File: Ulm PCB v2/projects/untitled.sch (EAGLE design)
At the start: 26 parts, among them U1 FT232RLSSOP, U2 MCP73831, U3 SPX3819-3.3, X2 USB-SMD-NS

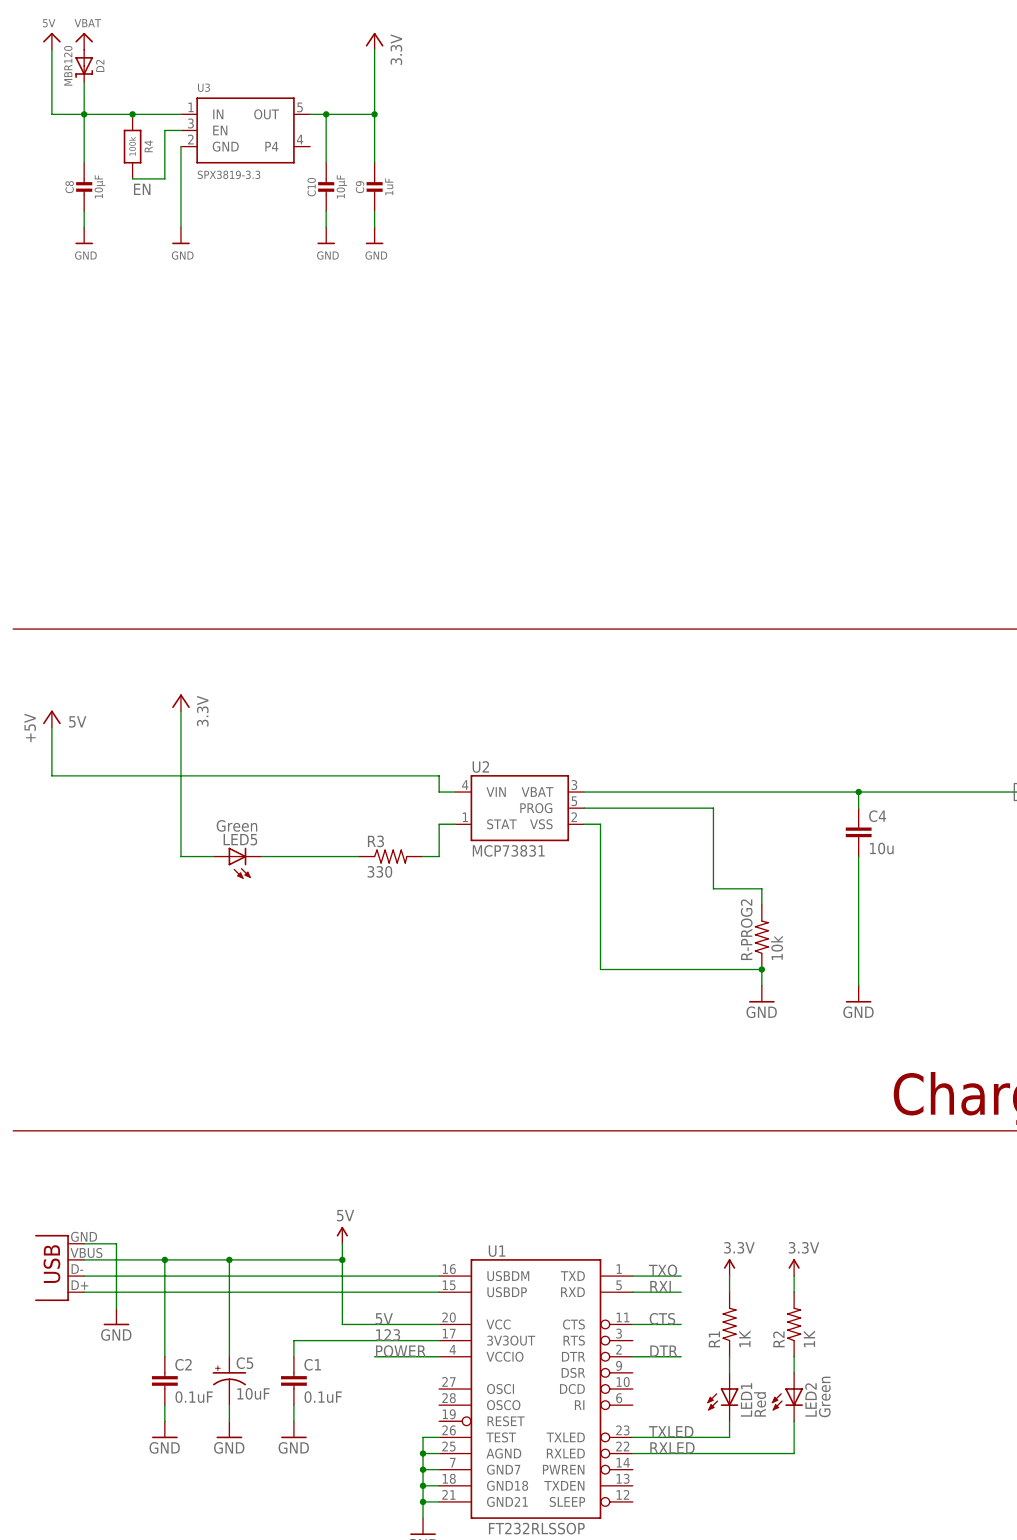
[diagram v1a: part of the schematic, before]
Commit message: replaced some parts with their bigger equivalent
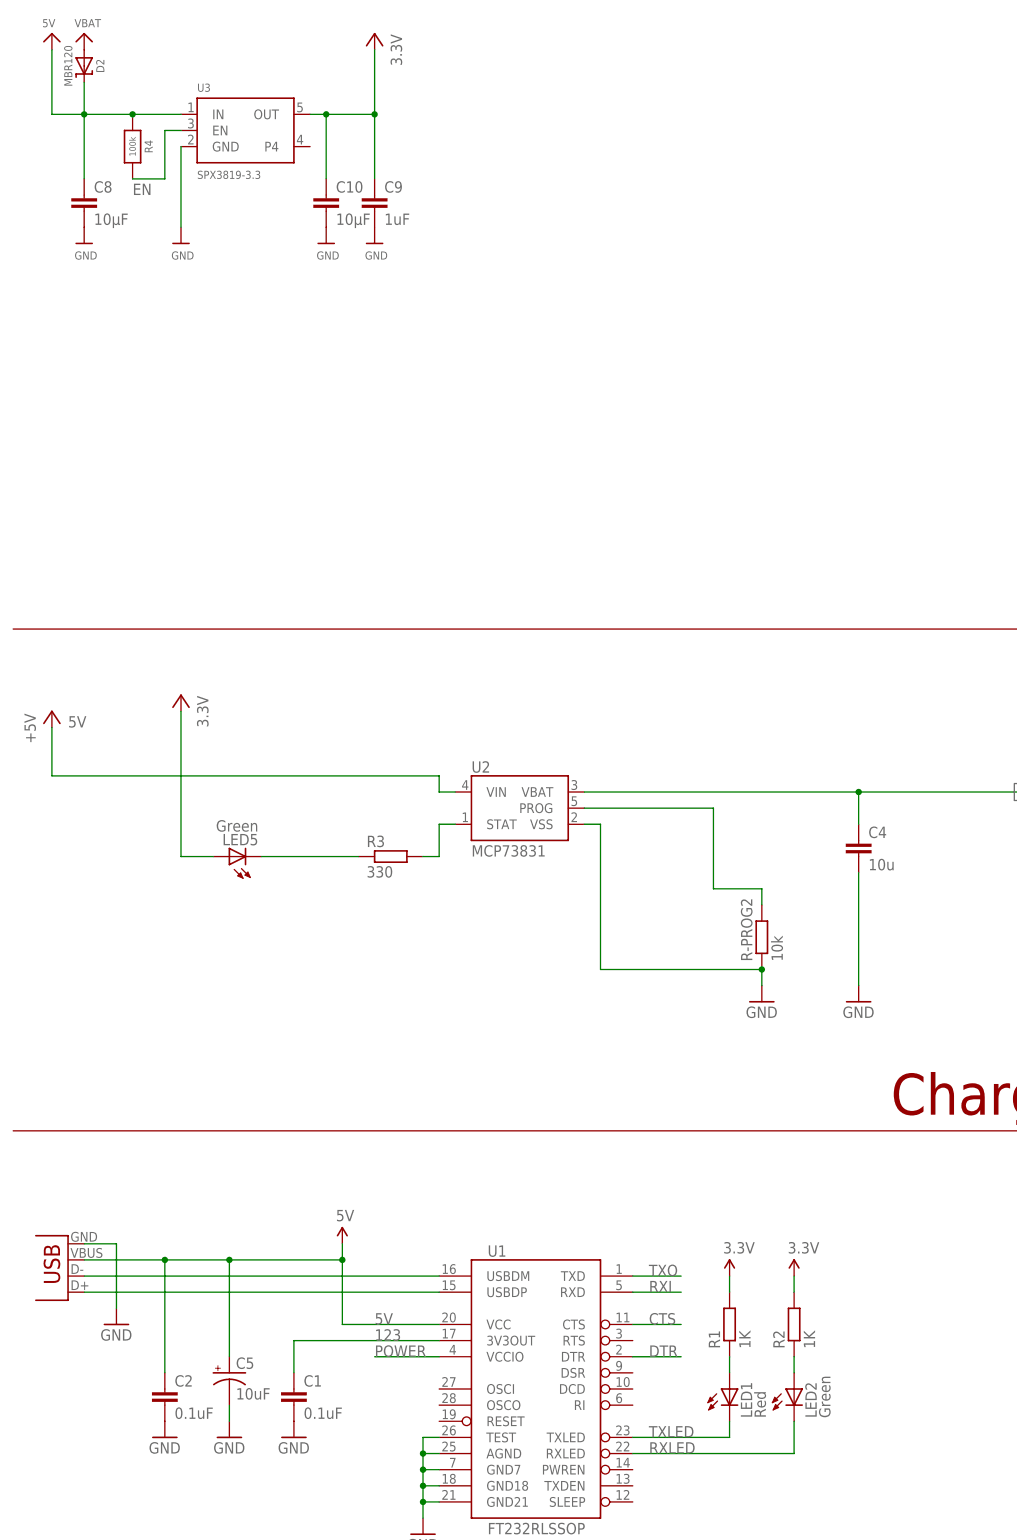
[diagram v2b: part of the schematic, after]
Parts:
- C1, C2: device SparkFun:CAP0402-CAP -> rcl:C-EUC0805
- C10, C8: device microbuilder:CAP_CERAMIC0805-NOOUTLINE -> rcl:C-EUC0805
- C4: device SparkFun-Capacitors:4.7UF-6.3V-10%(0603)0603 -> rcl:C-EUC0805
- C9: device microbuilder:CAP_CERAMIC0603_NO -> rcl:C-EUC0805
- R-PROG2: device SparkFun-Resistors:10KOHM1/10W1%(0603)0603 -> rcl:R-EU_R0603
- R1, R2: device SparkFun:RESISTOR0402-RES -> rcl:R-EU_R0603
- R3: device SparkFun-Resistors:330OHM1/10W1%(0603) -> rcl:R-EU_R0603
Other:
- moved on the sheet: C1, C10, C2, C4, C8, C9
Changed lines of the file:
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@@
 <part name="GND4" library="supply1" deviceset="GND" device=""/>
 <part name="GND6" library="supply1" deviceset="GND" device=""/>
-<part name="C2" library="SparkFun" deviceset="CAP" device="0402-CAP" value="0.1uF"/>
+<part name="C2" library="rcl" library_urn="urn:adsk.eagle:library:334" deviceset="C-EU" device="C0805" value="0.1uF"/>
 <part name="C5" library="SparkFun" deviceset="CAP_POL" device="1206" value="10uF"/>
-<part name="C1" library="SparkFun" deviceset="CAP" device="0402-CAP" value="0.1uF"/>
+<part name="C1" library="rcl" library_urn="urn:adsk.eagle:library:334" deviceset="C-EU" device="C0805" value="0.1uF"/>
 <part name="X2" library="SparkFun" deviceset="USB" device="-SMD-NS"/>
 <part name="GND2" library="SparkFun" deviceset="GND" device=""/>
@@
 <part name="GND7" library="SparkFun" deviceset="GND" device=""/>
 <part name="GND8" library="SparkFun" deviceset="GND" device=""/>
-<part name="R1" library="SparkFun" deviceset="RESISTOR" device="0402-RES" value="1K"/>
-<part name="R2" library="SparkFun" deviceset="RESISTOR" device="0402-RES" value="1K"/>
+<part name="R1" library="rcl" library_urn="urn:adsk.eagle:library:334" deviceset="R-EU_" device="R0603" value="1K"/>
+<part name="R2" library="rcl" library_urn="urn:adsk.eagle:library:334" deviceset="R-EU_" device="R0603" value="1K"/>
 <part name="LED1" library="SparkFun" deviceset="LED" device="0603" value="Red"/>
 <part name="LED2" library="SparkFun" deviceset="LED" device="0603" value="Green"/>
@@
 <part name="GND1" library="supply1" deviceset="GND" device=""/>
 <part name="U2" library="SparkFun-PowerIC" deviceset="MCP73831" device=""/>
-<part name="R3" library="SparkFun-Resistors" deviceset="330OHM1/10W1%(0603)" device="" value="330"/>
-<part name="C4" library="SparkFun-Capacitors" deviceset="4.7UF-6.3V-10%(0603)" device="0603" value="10u"/>
+<part name="R3" library="rcl" library_urn="urn:adsk.eagle:library:334" deviceset="R-EU_" device="R0603" value="330"/>
+<part name="C4" library="rcl" library_urn="urn:adsk.eagle:library:334" deviceset="C-EU" device="C0805" value="10u"/>
 <part name="GND12" library="SparkFun" deviceset="GND" device=""/>
-<part name="R-PROG2" library="SparkFun-Resistors" deviceset="10KOHM1/10W1%(0603)" device="0603" value="10k"/>
+<part name="R-PROG2" library="rcl" library_urn="urn:adsk.eagle:library:334" deviceset="R-EU_" device="R0603" value="10k"/>
 <part name="GND14" library="SparkFun" deviceset="GND" device=""/>
 <part name="FRAME1" library="frames" deviceset="A3L-LOC" device=""/>
@@
 <part name="GND9" library="supply1" deviceset="GND" device=""/>
 <part name="P+3" library="supply1" deviceset="VCC" device=""/>
-<part name="C6" library="rcl" deviceset="C-EU" device="C0805" value="100n"/>
+<part name="C6" library="rcl" library_urn="urn:adsk.eagle:library:334" deviceset="C-EU" device="C0805" value="100n"/>
 <part name="C7" library="rcl" deviceset="C-EU" device="C0805" value="100n"/>
 <part name="U$6" library="_c2h" deviceset="RFM95" device=""/>
@@
 <part name="GND13" library="supply1" deviceset="GND" device=""/>
 <part name="GND16" library="supply1" deviceset="GND" device=""/>
-<part name="C8" library="microbuilder" deviceset="CAP_CERAMIC" device="0805-NOOUTLINE" value="10µF"/>
-<part name="C9" library="microbuilder" deviceset="CAP_CERAMIC" device="0603_NO" value="1uF"/>
+<part name="C8" library="rcl" library_urn="urn:adsk.eagle:library:334" deviceset="C-EU" device="C0805" value="10µF"/>
+<part name="C9" library="rcl" library_urn="urn:adsk.eagle:library:334" deviceset="C-EU" device="C0805" value="1uF"/>
 <part name="U$27" library="microbuilder" deviceset="GND" device=""/>
 <part name="U$28" library="microbuilder" deviceset="GND" device=""/>
-<part name="C10" library="microbuilder" deviceset="CAP_CERAMIC" device="0805-NOOUTLINE" value="10µF"/>
+<part name="C10" library="rcl" library_urn="urn:adsk.eagle:library:334" deviceset="C-EU" device="C0805" value="10µF"/>
 <part name="U$29" library="microbuilder" deviceset="GND" device=""/>
 <part name="U$30" library="microbuilder" deviceset="GND" device=""/>
@@
 </segment>
 <segment>
-<wire x1="-121.92" y1="213.36" x2="-121.92" y2="210.82" width="0.1524" layer="91"/>
 <pinref part="GND2" gate="1" pin="GND"/>
 <pinref part="C1" gate="G$1" pin="2"/>
@@
 </segment>
 <segment>
-<wire x1="-142.24" y1="213.36" x2="-142.24" y2="210.82" width="0.1524" layer="91"/>
 <pinref part="C2" gate="G$1" pin="2"/>
 <pinref part="GND7" gate="1" pin="GND"/>
@@
 </segment>
 <segment>
-<wire x1="-33.02" y1="279.4" x2="-33.02" y2="299.72" width="0.1524" layer="91"/>
+<wire x1="-33.02" y1="279.4" x2="-33.02" y2="297.18" width="0.1524" layer="91"/>
 <pinref part="GND12" gate="1" pin="GND"/>
 <pinref part="C4" gate="G$1" pin="2"/>
@@
 <pinref part="C9" gate="G$1" pin="2"/>
 <pinref part="U$28" gate="G$1" pin="GND"/>
-<wire x1="-109.22" y1="401.32" x2="-109.22" y2="398.78" width="0.1524" layer="91"/>
 </segment>
 <segment>
 <pinref part="C8" gate="G$1" pin="2"/>
 <pinref part="U$27" gate="G$1" pin="GND"/>
-<wire x1="-154.94" y1="401.32" x2="-154.94" y2="398.78" width="0.1524" layer="91"/>
 </segment>
 <segment>
 <pinref part="C10" gate="G$1" pin="2"/>
 <pinref part="U$29" gate="G$1" pin="GND"/>
-<wire x1="-116.84" y1="401.32" x2="-116.84" y2="398.78" width="0.1524" layer="91"/>
 </segment>
 <segment>
@@
 <wire x1="-109.22" y1="416.56" x2="-109.22" y2="426.72" width="0.1524" layer="91"/>
 <pinref part="C9" gate="G$1" pin="1"/>
-<wire x1="-109.22" y1="416.56" x2="-109.22" y2="408.94" width="0.1524" layer="91"/>
+<wire x1="-109.22" y1="416.56" x2="-109.22" y2="406.4" width="0.1524" layer="91"/>
 <junction x="-109.22" y="416.56"/>
 <pinref part="C10" gate="G$1" pin="1"/>
-<wire x1="-116.84" y1="408.94" x2="-116.84" y2="416.56" width="0.1524" layer="91"/>
+<wire x1="-116.84" y1="406.4" x2="-116.84" y2="416.56" width="0.1524" layer="91"/>
 <junction x="-116.84" y="416.56"/>
 <pinref part="+3V4" gate="G$1" pin="+3V3"/>
@@
 <wire x1="-114.3" y1="226.06" x2="-99.06" y2="226.06" width="0.1524" layer="91"/>
 <wire x1="-132.08" y1="220.98" x2="-132.08" y2="236.22" width="0.1524" layer="91"/>
-<wire x1="-142.24" y1="220.98" x2="-142.24" y2="236.22" width="0.1524" layer="91"/>
+<wire x1="-142.24" y1="218.44" x2="-142.24" y2="236.22" width="0.1524" layer="91"/>
 <wire x1="-154.94" y1="236.22" x2="-142.24" y2="236.22" width="0.1524" layer="91"/>
 <wire x1="-114.3" y1="238.76" x2="-114.3" y2="236.22" width="0.1524" layer="91"/>
@@
 <wire x1="-139.7" y1="416.56" x2="-147.32" y2="416.56" width="0.1524" layer="91"/>
 <wire x1="-147.32" y1="416.56" x2="-154.94" y2="416.56" width="0.1524" layer="91"/>
-<wire x1="-154.94" y1="416.56" x2="-154.94" y2="408.94" width="0.1524" layer="91"/>
+<wire x1="-154.94" y1="416.56" x2="-154.94" y2="406.4" width="0.1524" layer="91"/>
 <wire x1="-154.94" y1="421.64" x2="-154.94" y2="416.56" width="0.1524" layer="91"/>
 <pinref part="U3" gate="G$1" pin="IN"/>
@@
 <segment>
 <pinref part="C4" gate="G$1" pin="1"/>
-<wire x1="-33.02" y1="309.88" x2="-33.02" y2="307.34" width="0.1524" layer="91"/>
+<wire x1="-33.02" y1="309.88" x2="-33.02" y2="304.8" width="0.1524" layer="91"/>
 <wire x1="-76.2" y1="309.88" x2="-33.02" y2="309.88" width="0.1524" layer="91"/>
 <pinref part="U2" gate="G$1" pin="VBAT"/>
@@
 <segment>
 <wire x1="-99.06" y1="223.52" x2="-121.92" y2="223.52" width="0.1524" layer="91"/>
-<wire x1="-121.92" y1="223.52" x2="-121.92" y2="220.98" width="0.1524" layer="91"/>
+<wire x1="-121.92" y1="223.52" x2="-121.92" y2="218.44" width="0.1524" layer="91"/>
 <label x="-109.22" y="223.52" size="1.778" layer="95"/>
 <pinref part="U1" gate="G$1" pin="3V3OUT"/>
@@
 </schematic>
 </drawing>
+<compatibility>
+<note version="8.2" severity="warning">
+Since Version 8.2, Eagle supports online libraries. The ids
+of those online libraries will not be understood (or retained)
+with this version.
+</note>
+</compatibility>
 </eagle>
